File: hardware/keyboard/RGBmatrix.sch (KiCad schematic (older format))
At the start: 44 parts

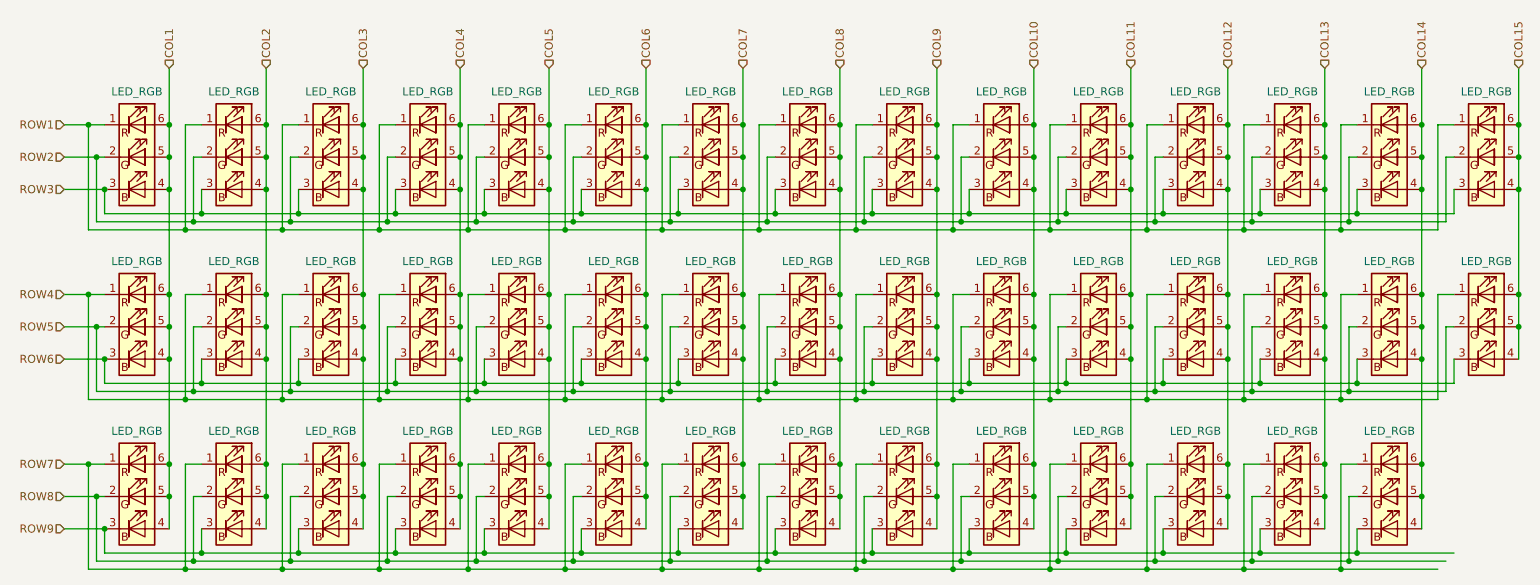
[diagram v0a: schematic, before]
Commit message: switch to proper type of RGB(Common anode)
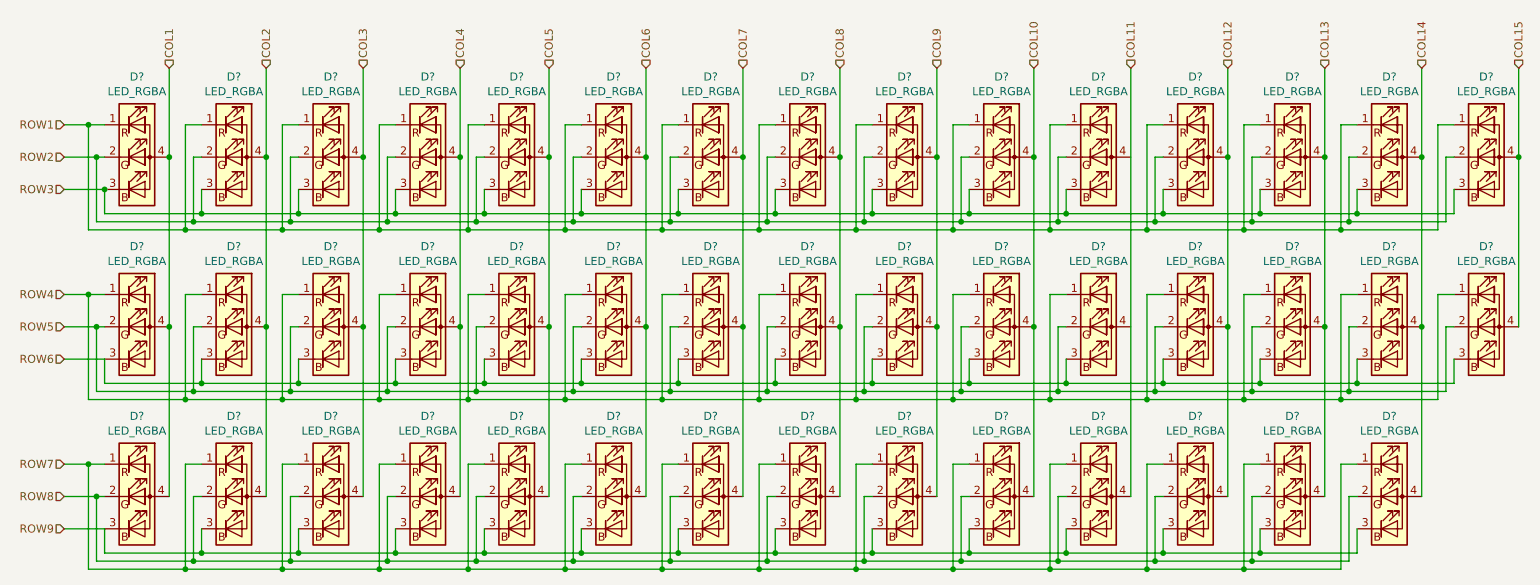
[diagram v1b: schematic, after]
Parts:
- removed D100, D101, D102, D103, D104, D105, D106, D107, D108, D109, D110, D111, D112, D69, D70, D71, D72, D73, D74, D75, D76, D77, D78, D79, D80, D81, D82, D83, D84, D85, D86, D87, D88, D89, D90, D91, D92, D93, D94, D95, D96, D97, D98, D99: LED_RGB, symbol Device:LED_RGB
- added D? (x44): LED_RGBA, symbol Device:LED_RGBA
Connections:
- net COL1: now also D?.4 (A), D?.4 (A), D?.4 (A)
- net COL10: now also D?.4 (A), D?.4 (A), D?.4 (A)
- net COL11: now also D?.4 (A)
- net COL12: now also D?.4 (A), D?.4 (A), D?.4 (A)
- net COL13: now also D?.4 (A), D?.4 (A), D?.4 (A)
- net COL14: now also D?.4 (A), D?.4 (A), D?.4 (A)
- net COL15: now also D?.4 (A), D?.4 (A)
- net COL2: now also D?.4 (A), D?.4 (A), D?.4 (A)
- net COL3: now also D?.4 (A), D?.4 (A), D?.4 (A)
- net COL4: now also D?.4 (A), D?.4 (A), D?.4 (A)
- net COL5: now also D?.4 (A), D?.4 (A), D?.4 (A)
- net COL6: now also D?.4 (A), D?.4 (A), D?.4 (A)
- net COL7: now also D?.4 (A), D?.4 (A), D?.4 (A)
- net COL8: now also D?.4 (A), D?.4 (A), D?.4 (A)
- net COL9: now also D?.4 (A), D?.4 (A), D?.4 (A)
- net ROW1: now also D?.1 (RK), D?.1 (RK), D?.1 (RK), D?.1 (RK), D?.1 (RK), D?.1 (RK), D?.1 (RK), D?.1 (RK), D?.1 (RK), D?.1 (RK), D?.1 (RK), D?.1 (RK), D?.1 (RK), D?.1 (RK), D?.1 (RK)
- net ROW2: now also D?.2 (GK), D?.2 (GK), D?.2 (GK), D?.2 (GK), D?.2 (GK), D?.2 (GK), D?.2 (GK), D?.2 (GK), D?.2 (GK), D?.2 (GK), D?.2 (GK), D?.2 (GK), D?.2 (GK), D?.2 (GK), D?.2 (GK)
- net ROW3: now also D?.3 (BK), D?.3 (BK), D?.3 (BK), D?.3 (BK), D?.3 (BK), D?.3 (BK), D?.3 (BK), D?.3 (BK), D?.3 (BK), D?.3 (BK), D?.3 (BK), D?.3 (BK), D?.3 (BK), D?.3 (BK), D?.3 (BK)
- net ROW4: now also D?.1 (RK), D?.1 (RK), D?.1 (RK), D?.1 (RK), D?.1 (RK), D?.1 (RK), D?.1 (RK), D?.1 (RK), D?.1 (RK), D?.1 (RK), D?.1 (RK), D?.1 (RK), D?.1 (RK), D?.1 (RK), D?.1 (RK)
- net ROW5: now also D?.2 (GK), D?.2 (GK), D?.2 (GK), D?.2 (GK), D?.2 (GK), D?.2 (GK), D?.2 (GK), D?.2 (GK), D?.2 (GK), D?.2 (GK), D?.2 (GK), D?.2 (GK), D?.2 (GK), D?.2 (GK), D?.2 (GK)
- net ROW6: now also D?.3 (BK), D?.3 (BK), D?.3 (BK), D?.3 (BK), D?.3 (BK), D?.3 (BK), D?.3 (BK), D?.3 (BK), D?.3 (BK), D?.3 (BK), D?.3 (BK), D?.3 (BK), D?.3 (BK), D?.3 (BK), D?.3 (BK)
- net ROW7: now also D?.1 (RK), D?.1 (RK), D?.1 (RK), D?.1 (RK), D?.1 (RK), D?.1 (RK), D?.1 (RK), D?.1 (RK), D?.1 (RK), D?.1 (RK), D?.1 (RK), D?.1 (RK), D?.1 (RK), D?.1 (RK)
- net ROW8: now also D?.2 (GK), D?.2 (GK), D?.2 (GK), D?.2 (GK), D?.2 (GK), D?.2 (GK), D?.2 (GK), D?.2 (GK), D?.2 (GK), D?.2 (GK), D?.2 (GK), D?.2 (GK), D?.2 (GK), D?.2 (GK)
- net ROW9: now also D?.3 (BK), D?.3 (BK), D?.3 (BK), D?.3 (BK), D?.3 (BK), D?.3 (BK), D?.3 (BK), D?.3 (BK), D?.3 (BK), D?.3 (BK), D?.3 (BK), D?.3 (BK), D?.3 (BK), D?.3 (BK)

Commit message: fix unconnected rgb
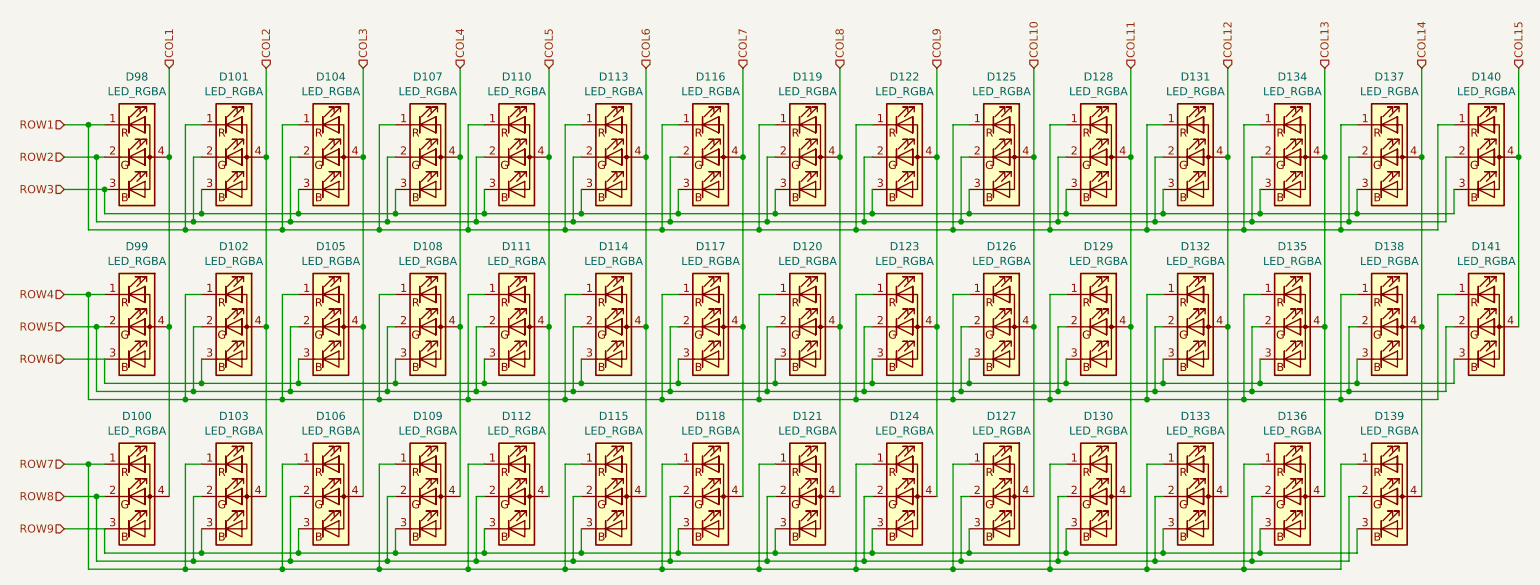
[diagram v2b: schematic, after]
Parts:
- gave numbers to parts that had none: 44
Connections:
- net COL11: now also D128.4 (A), D129.4 (A)

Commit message: now it should be using the correct rgb symbol (RABG)
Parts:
- D100, D101, D102, D103, D104, D105, D106, D107, D108, D109, D110, D111, D112, D113, D114, D115, D116, D117, D118, D119, D120, D121, D122, D123, D124, D125, D126, D127, D128, D129, D130, D131, D132, D133, D134, D135, D136, D137, D138, D139, D140, D141, D98, D99: value LED_RGBA -> LED_RABG; symbol Device:LED_RGBA -> Device:LED_RABG
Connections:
- net COL1: now also D100.2 (A), D98.2 (A), D99.2 (A); no longer D100.4 (A), D98.4 (A), D99.4 (A)
- net COL10: now also D125.2 (A), D126.2 (A), D127.2 (A); no longer D125.4 (A), D126.4 (A), D127.4 (A)
- net COL11: now also D128.2 (A), D129.2 (A), D130.2 (A); no longer D128.4 (A), D129.4 (A), D130.4 (A)
- net COL12: now also D131.2 (A), D132.2 (A), D133.2 (A); no longer D131.4 (A), D132.4 (A), D133.4 (A)
- net COL13: now also D134.2 (A), D135.2 (A), D136.2 (A); no longer D134.4 (A), D135.4 (A), D136.4 (A)
- net COL14: now also D137.2 (A), D138.2 (A), D139.2 (A); no longer D137.4 (A), D138.4 (A), D139.4 (A)
- net COL15: now also D140.2 (A), D141.2 (A); no longer D140.4 (A), D141.4 (A)
- net COL2: now also D101.2 (A), D102.2 (A), D103.2 (A); no longer D101.4 (A), D102.4 (A), D103.4 (A)
- net COL3: now also D104.2 (A), D105.2 (A), D106.2 (A); no longer D104.4 (A), D105.4 (A), D106.4 (A)
- net COL4: now also D107.2 (A), D108.2 (A), D109.2 (A); no longer D107.4 (A), D108.4 (A), D109.4 (A)
- net COL5: now also D110.2 (A), D111.2 (A), D112.2 (A); no longer D110.4 (A), D111.4 (A), D112.4 (A)
- net COL6: now also D113.2 (A), D114.2 (A), D115.2 (A); no longer D113.4 (A), D114.4 (A), D115.4 (A)
- net COL7: now also D116.2 (A), D117.2 (A), D118.2 (A); no longer D116.4 (A), D117.4 (A), D118.4 (A)
- net COL8: now also D119.2 (A), D120.2 (A), D121.2 (A); no longer D119.4 (A), D120.4 (A), D121.4 (A)
- net COL9: now also D122.2 (A), D123.2 (A), D124.2 (A); no longer D122.4 (A), D123.4 (A), D124.4 (A)
- net ROW2: now also D101.4 (GK), D104.4 (GK), D107.4 (GK), D110.4 (GK), D113.4 (GK), D116.4 (GK), D119.4 (GK), D122.4 (GK), D125.4 (GK), D128.4 (GK), D131.4 (GK), D134.4 (GK), D137.4 (GK), D140.4 (GK), D98.4 (GK); no longer D101.2 (GK), D104.2 (GK), D107.2 (GK), D110.2 (GK), D113.2 (GK), D116.2 (GK), D119.2 (GK), D122.2 (GK), D125.2 (GK), D128.2 (GK), D131.2 (GK), D134.2 (GK), D137.2 (GK), D140.2 (GK), D98.2 (GK)
- net ROW5: now also D102.4 (GK), D105.4 (GK), D108.4 (GK), D111.4 (GK), D114.4 (GK), D117.4 (GK), D120.4 (GK), D123.4 (GK), D126.4 (GK), D129.4 (GK), D132.4 (GK), D135.4 (GK), D138.4 (GK), D141.4 (GK), D99.4 (GK); no longer D102.2 (GK), D105.2 (GK), D108.2 (GK), D111.2 (GK), D114.2 (GK), D117.2 (GK), D120.2 (GK), D123.2 (GK), D126.2 (GK), D129.2 (GK), D132.2 (GK), D135.2 (GK), D138.2 (GK), D141.2 (GK), D99.2 (GK)
- net ROW8: now also D100.4 (GK), D103.4 (GK), D106.4 (GK), D109.4 (GK), D112.4 (GK), D115.4 (GK), D118.4 (GK), D121.4 (GK), D124.4 (GK), D127.4 (GK), D130.4 (GK), D133.4 (GK), D136.4 (GK), D139.4 (GK); no longer D100.2 (GK), D103.2 (GK), D106.2 (GK), D109.2 (GK), D112.2 (GK), D115.2 (GK), D118.2 (GK), D121.2 (GK), D124.2 (GK), D127.2 (GK), D130.2 (GK), D133.2 (GK), D136.2 (GK), D139.2 (GK)

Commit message: use proper footprint, link symbols and footprints
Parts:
- D100, D101, D102, D103, D104, D105, D106, D107, D108, D109, D110, D111, D112, D113, D114, D115, D116, D117, D118, D119, D120, D121, D122, D123, D124, D125, D126, D127, D128, D129, D130, D131, D132, D133, D134, D135, D136, D137, D138, D139, D140, D141, D98, D99: footprint (none) -> KiCad:XZMDKCBDDG45S9
